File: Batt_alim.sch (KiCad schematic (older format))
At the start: 4 parts

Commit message: added battery footprint
and some net names
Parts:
- BT?: footprint (none) -> Battery:BatteryHolder_Keystone_1042_1x18650
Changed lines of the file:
@@
 F 0 "BT?" H 4718 3896 50  0000 L CNN
 F 1 "Battery_Cell" H 4718 3805 50  0000 L CNN
-F 2 "" V 4600 3860 50  0001 C CNN
+F 2 "Battery:BatteryHolder_Keystone_1042_1x18650" V 4600 3860 50  0001 C CNN
 F 3 "~" V 4600 3860 50  0001 C CNN
 	1    4600 3800

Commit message: fin schéma, début placement
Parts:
- gave numbers to parts that had none: 4
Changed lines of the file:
@@
 $EndDescr
 $Comp
-L Chimere:Batt_Alim U?
+L Chimere:Batt_Alim U4
 U 1 1 5FDF7692
 P 6300 3750
-F 0 "U?" H 6300 4290 50  0000 C CNN
+F 0 "U4" H 6300 4290 50  0000 C CNN
 F 1 "Batt_Alim" H 6300 4199 50  0000 C CNN
 F 2 "Chimere:Batt_Alim" H 6300 3750 50  0001 C CNN
@@
 	5325 3700 5800 3700
 $Comp
-L Connector_Generic:Conn_01x03 J?
+L Connector_Generic:Conn_01x03 J28
 U 1 1 5FDF9A30
-P 5800 4425
-F 0 "J?" H 5718 4100 50  0000 C CNN
-F 1 "Conn_01x03" H 5718 4191 50  0000 C CNN
-F 2 "Connector_JST:JST_XH_S3B-XH-A_1x03_P2.50mm_Horizontal" H 5800 4425 50  0001 C CNN
-F 3 "~" H 5800 4425 50  0001 C CNN
-	1    5800 4425
-	0    1    1    0
+P 5700 4425
+F 0 "J28" H 5618 4100 50  0000 C CNN
+F 1 "Conn_01x03" H 5618 4191 50  0000 C CNN
+F 2 "Connector_JST:JST_XH_S3B-XH-A_1x03_P2.50mm_Horizontal" H 5700 4425 50  0001 C CNN
+F 3 "~" H 5700 4425 50  0001 C CNN
+	1    5700 4425
+	0    -1   1    0
 $EndComp
-NoConn ~ 5900 4225
 $Comp
 L Connector_Generic:Conn_01x02 J?
@@
 P 5100 3200
 AR Path="/5FC6C772/5FDFAD94" Ref="J?"  Part="1"
-AR Path="/5FC6D1FC/5FDFAD94" Ref="J?"  Part="1"
-F 0 "J?" H 5018 2875 50  0000 C CNN
+AR Path="/5FC6D1FC/5FDFAD94" Ref="J27"  Part="1"
+F 0 "J27" H 5018 2875 50  0000 C CNN
 F 1 "Conn_01x02" H 5018 2966 50  0000 C CNN
 F 2 "Connector_JST:JST_XH_B2B-XH-A_1x02_P2.50mm_Vertical" H 5100 3200 50  0001 C CNN
@@
 	5700 3950 5700 4225
 $Comp
-L Device:Battery_Cell BT?
+L Device:Battery_Cell BT1
 U 1 1 5FDFD2B1
 P 4600 3800
-F 0 "BT?" H 4718 3896 50  0000 L CNN
+F 0 "BT1" H 4718 3896 50  0000 L CNN
 F 1 "Battery_Cell" H 4718 3805 50  0000 L CNN
 F 2 "Battery:BatteryHolder_Keystone_1042_1x18650" V 4600 3860 50  0001 C CNN
@@
 Wire Wire Line
 	5325 3825 5800 3825
+NoConn ~ 5600 4225
 $EndSCHEMATC

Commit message: routing + generation gerber
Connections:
- net labels added: V_ext
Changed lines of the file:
@@
 L Connector_Generic:Conn_01x03 J28
 U 1 1 5FDF9A30
-P 5700 4425
-F 0 "J28" H 5618 4100 50  0000 C CNN
-F 1 "Conn_01x03" H 5618 4191 50  0000 C CNN
-F 2 "Connector_JST:JST_XH_S3B-XH-A_1x03_P2.50mm_Horizontal" H 5700 4425 50  0001 C CNN
-F 3 "~" H 5700 4425 50  0001 C CNN
-	1    5700 4425
-	0    -1   1    0
+P 5800 4425
+F 0 "J28" H 5718 4100 50  0000 C CNN
+F 1 "Conn_01x03" H 5718 4191 50  0000 C CNN
+F 2 "Connector_JST:JST_XH_S3B-XH-A_1x03_P2.50mm_Horizontal" H 5800 4425 50  0001 C CNN
+F 3 "~" H 5800 4425 50  0001 C CNN
+	1    5800 4425
+	0    1    1    0
 $EndComp
 $Comp
@@
 Wire Wire Line
 	5325 3825 5800 3825
-NoConn ~ 5600 4225
+NoConn ~ 5900 4225
+Text Label 5575 3100 0    50   ~ 0
+V_ext
 $EndSCHEMATC

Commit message: maj
simplification dfr
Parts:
- removed BT1: Battery_Cell, Battery:BatteryHolder_Keystone_1042_1x18650, symbol Device:Battery_Cell
- removed J28: Conn_01x03, Connector_JST:JST_XH_S3B-XH-A_1x03_P2.50mm_Horizontal, symbol Connector_Generic:Conn_01x03
- added J4, J9: Conn_01x02, Connector_JST:JST_XH_B2B-XH-A_1x02_P2.50mm_Vertical, symbol Connector_Generic:Conn_01x02
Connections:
- net labels removed: 3V3, V_2_uC, uC_2_V
- wire segments 19 -> 8
- no-connect marks 1 -> 0
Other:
- note added: "G3T12AH-R"
- note added: "connecteur batterie\n"
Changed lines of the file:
@@
 $Descr A4 11693 8268
 encoding utf-8
-Sheet 5 5
+Sheet 5 6
 Title ""
 Date ""
@@
 	1    0    0    -1
 $EndComp
-Text GLabel 6950 3575 2    50   Input ~ 0
-GND
 Text GLabel 6950 3450 2    50   Input ~ 0
 5V
 Wire Wire Line
 	6800 3450 6950 3450
-Text GLabel 6950 4075 2    50   Input ~ 0
-GND
 Text GLabel 5700 3575 0    50   Input ~ 0
 GND
 Wire Wire Line
-	6800 3575 6950 3575
-Wire Wire Line
-	6800 4075 6950 4075
-Wire Wire Line
 	5700 3575 5800 3575
-Text GLabel 6950 3825 2    50   Input ~ 0
-V_2_uC
-Text GLabel 6950 3950 2    50   Input ~ 0
-uC_2_V
-Wire Wire Line
-	6800 3825 6950 3825
-Wire Wire Line
-	6800 3950 6950 3950
-Text GLabel 6950 3700 2    50   Input ~ 0
-3V3
-Wire Wire Line
-	6800 3700 6950 3700
-Wire Wire Line
-	5325 3700 5800 3700
-$Comp
-L Connector_Generic:Conn_01x03 J28
-U 1 1 5FDF9A30
-P 5800 4425
-F 0 "J28" H 5718 4100 50  0000 C CNN
-F 1 "Conn_01x03" H 5718 4191 50  0000 C CNN
-F 2 "Connector_JST:JST_XH_S3B-XH-A_1x03_P2.50mm_Horizontal" H 5800 4425 50  0001 C CNN
-F 3 "~" H 5800 4425 50  0001 C CNN
-	1    5800 4425
-	0    1    1    0
-$EndComp
 $Comp
 L Connector_Generic:Conn_01x02 J?
@@
 Text Notes 3675 3175 0    50   ~ 0
 connecteur alimentation extérieure
-Text Notes 6050 4700 2    50   ~ 0
+Text Notes 5750 4175 2    50   ~ 0
 connecteur interrupteur
-Wire Wire Line
-	5800 4075 5800 4225
-Wire Wire Line
-	5800 3950 5700 3950
-Wire Wire Line
-	5700 3950 5700 4225
-$Comp
-L Device:Battery_Cell BT1
-U 1 1 5FDFD2B1
-P 4600 3800
-F 0 "BT1" H 4718 3896 50  0000 L CNN
-F 1 "Battery_Cell" H 4718 3805 50  0000 L CNN
-F 2 "Battery:BatteryHolder_Keystone_1042_1x18650" V 4600 3860 50  0001 C CNN
-F 3 "~" V 4600 3860 50  0001 C CNN
-	1    4600 3800
-	1    0    0    -1
-$EndComp
-Wire Wire Line
-	4600 3600 5325 3600
-Wire Wire Line
-	5325 3600 5325 3700
-Wire Wire Line
-	4600 3900 5325 3900
-Wire Wire Line
-	5325 3900 5325 3825
-Wire Wire Line
-	5325 3825 5800 3825
-NoConn ~ 5900 4225
 Text Label 5575 3100 0    50   ~ 0
 V_ext
+Text Notes 5900 4175 0    50   ~ 0
+G3T12AH-R
+$Comp
+L Connector_Generic:Conn_01x02 J?
+U 1 1 6031A76D
+P 5500 3900
+AR Path="/5FC6C772/6031A76D" Ref="J?"  Part="1"
+AR Path="/5FC6D1FC/6031A76D" Ref="J9"  Part="1"
+F 0 "J9" H 5418 3575 50  0000 C CNN
+F 1 "Conn_01x02" H 5418 3666 50  0000 C CNN
+F 2 "Connector_JST:JST_XH_B2B-XH-A_1x02_P2.50mm_Vertical" H 5500 3900 50  0001 C CNN
+F 3 "~" H 5500 3900 50  0001 C CNN
+	1    5500 3900
+	0    1    1    0
+$EndComp
+$Comp
+L Connector_Generic:Conn_01x02 J?
+U 1 1 6031BF0F
+P 4550 3800
+AR Path="/5FC6C772/6031BF0F" Ref="J?"  Part="1"
+AR Path="/5FC6D1FC/6031BF0F" Ref="J4"  Part="1"
+F 0 "J4" H 4468 3475 50  0000 C CNN
+F 1 "Conn_01x02" H 4468 3566 50  0000 C CNN
+F 2 "Connector_JST:JST_XH_B2B-XH-A_1x02_P2.50mm_Vertical" H 4550 3800 50  0001 C CNN
+F 3 "~" H 4550 3800 50  0001 C CNN
+	1    4550 3800
+	-1   0    0    1
+$EndComp
+Text Notes 3700 3775 0    50   ~ 0
+connecteur batterie\n
+Text GLabel 4850 3800 2    50   Input ~ 0
+GND
+Wire Wire Line
+	5800 3700 5500 3700
+Wire Wire Line
+	5400 3700 4750 3700
+Wire Wire Line
+	4750 3800 4850 3800
 $EndSCHEMATC

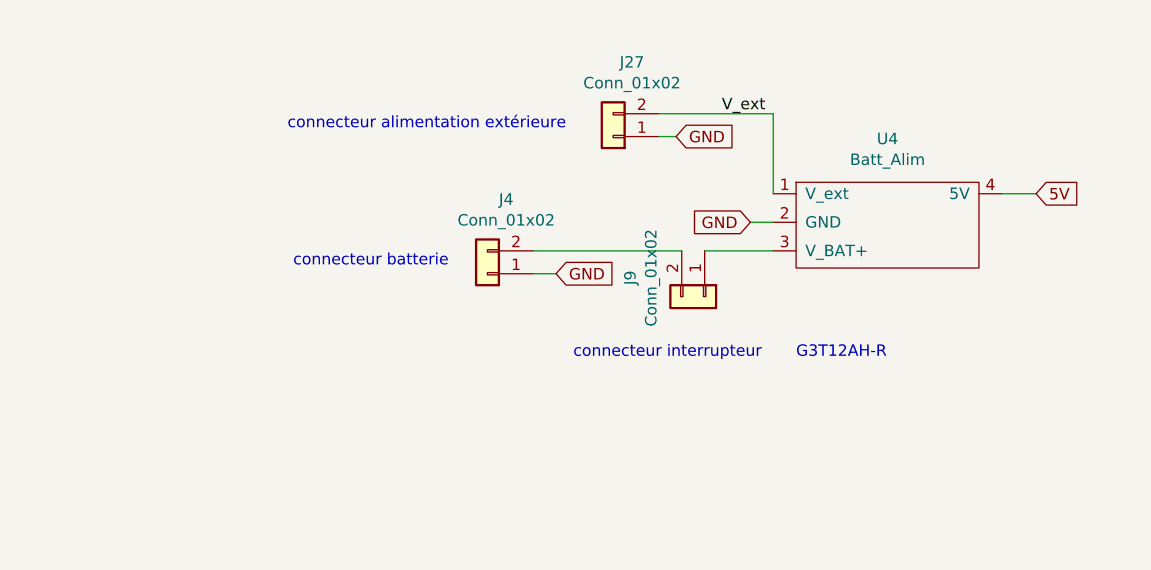
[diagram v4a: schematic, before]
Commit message: changement connecteur
utilisation d'un connecteur usb micro pour l'alimentation
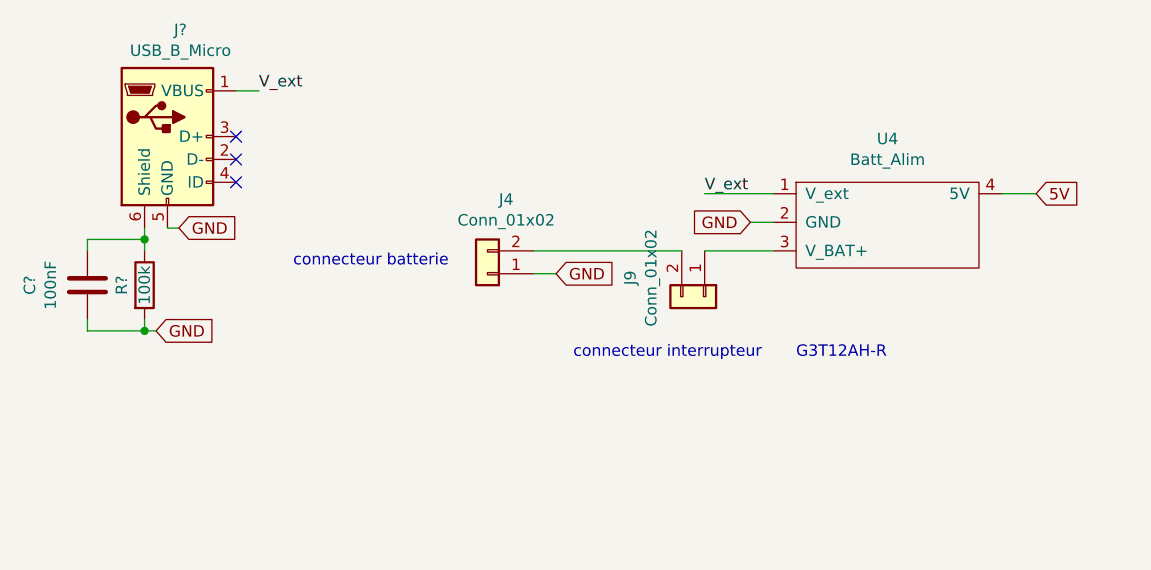
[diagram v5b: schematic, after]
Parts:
- removed J27: Conn_01x02, Connector_JST:JST_XH_B2B-XH-A_1x02_P2.50mm_Vertical, symbol Connector_Generic:Conn_01x02
- added C?: 100nF, Capacitor_SMD:C_0603_1608Metric_Pad1.05x0.95mm_HandSolder, symbol Device:C
- added J?: USB_B_Micro, Connector_USB:USB_Micro-B_Wuerth_629105150521_CircularHoles, symbol Connector:USB_B_Micro
- added R?: 100k, Resistor_SMD:R_0603_1608Metric_Pad1.05x0.95mm_HandSolder, symbol Device:R
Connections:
- net GND: now also C?.2, J?.5 (GND), R?.2
- net V_ext: now also J?.1 (VBUS)
- new net: C?.1, J?.6 (Shield), R?.1
- no-connect marks 0 -> 3
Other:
- note removed: "connecteur alimentation extérieure"
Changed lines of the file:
@@
 Wire Wire Line
 	5700 3575 5800 3575
-$Comp
-L Connector_Generic:Conn_01x02 J?
-U 1 1 5FDFAD94
-P 5100 3200
-AR Path="/5FC6C772/5FDFAD94" Ref="J?"  Part="1"
-AR Path="/5FC6D1FC/5FDFAD94" Ref="J27"  Part="1"
-F 0 "J27" H 5018 2875 50  0000 C CNN
-F 1 "Conn_01x02" H 5018 2966 50  0000 C CNN
-F 2 "Connector_JST:JST_XH_B2B-XH-A_1x02_P2.50mm_Vertical" H 5100 3200 50  0001 C CNN
-F 3 "~" H 5100 3200 50  0001 C CNN
-	1    5100 3200
-	-1   0    0    1
-$EndComp
-Text GLabel 5375 3200 2    50   Input ~ 0
-GND
-Wire Wire Line
-	5300 3200 5375 3200
-Wire Wire Line
-	5300 3100 5800 3100
-Wire Wire Line
-	5800 3100 5800 3450
-Text Notes 3675 3175 0    50   ~ 0
-connecteur alimentation extérieure
 Text Notes 5750 4175 2    50   ~ 0
 connecteur interrupteur
-Text Label 5575 3100 0    50   ~ 0
+Text Label 5500 3450 0    50   ~ 0
 V_ext
 Text Notes 5900 4175 0    50   ~ 0
@@
 Wire Wire Line
 	4750 3800 4850 3800
+$Comp
+L Device:R R?
+U 1 1 606BFC88
+P 3050 3850
+AR Path="/5FC6D1B4/606BFC88" Ref="R?"  Part="1"
+AR Path="/5FC6C772/606BFC88" Ref="R?"  Part="1"
+AR Path="/5FC6D1FC/606BFC88" Ref="R?"  Part="1"
+F 0 "R?" V 2950 3850 50  0000 C CNN
+F 1 "100k" V 3050 3850 50  0000 C CNN
+F 2 "Resistor_SMD:R_0603_1608Metric_Pad1.05x0.95mm_HandSolder" V 2980 3850 50  0001 C CNN
+F 3 "~" H 3050 3850 50  0001 C CNN
+	1    3050 3850
+	1    0    0    -1
+$EndComp
+$Comp
+L Device:C C?
+U 1 1 606BFC8E
+P 2800 3850
+AR Path="/5FC6C772/606BFC8E" Ref="C?"  Part="1"
+AR Path="/5FC6D1FC/606BFC8E" Ref="C?"  Part="1"
+F 0 "C?" V 2548 3850 50  0000 C CNN
+F 1 "100nF" V 2639 3850 50  0000 C CNN
+F 2 "Capacitor_SMD:C_0603_1608Metric_Pad1.05x0.95mm_HandSolder" H 2838 3700 50  0001 C CNN
+F 3 "C14663" H 2800 3850 50  0001 C CNN
+	1    2800 3850
+	1    0    0    -1
+$EndComp
+Text GLabel 3200 3600 2    50   Input ~ 0
+GND
+Wire Wire Line
+	3150 3600 3200 3600
+Wire Wire Line
+	3050 3700 3050 3650
+Wire Wire Line
+	2800 3700 2800 3650
+Wire Wire Line
+	2800 3650 3050 3650
+Connection ~ 3050 3650
+Wire Wire Line
+	3050 3650 3050 3600
+Wire Wire Line
+	2800 4000 2800 4050
+Wire Wire Line
+	2800 4050 3050 4050
+Wire Wire Line
+	3050 4050 3050 4000
+Text GLabel 3100 4050 2    50   Input ~ 0
+GND
+Wire Wire Line
+	3100 4050 3050 4050
+Connection ~ 3050 4050
+NoConn ~ 3450 3200
+NoConn ~ 3450 3300
+Text Label 3550 3000 0    50   ~ 0
+V_ext
+Wire Wire Line
+	3550 3000 3450 3000
+Wire Wire Line
+	5500 3450 5800 3450
+NoConn ~ 3450 3400
+$Comp
+L Connector:USB_B_Micro J?
+U 1 1 606C5F07
+P 3150 3200
+F 0 "J?" H 3207 3667 50  0000 C CNN
+F 1 "USB_B_Micro" H 3207 3576 50  0000 C CNN
+F 2 "Connector_USB:USB_Micro-B_Wuerth_629105150521_CircularHoles" H 3300 3150 50  0001 C CNN
+F 3 "~" H 3300 3150 50  0001 C CNN
+	1    3150 3200
+	1    0    0    -1
+$EndComp
 $EndSCHEMATC

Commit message: modification audio + alim
utilisation du module Audio_Facile
+ utilisation d'un rotary switch rotary potentiometer
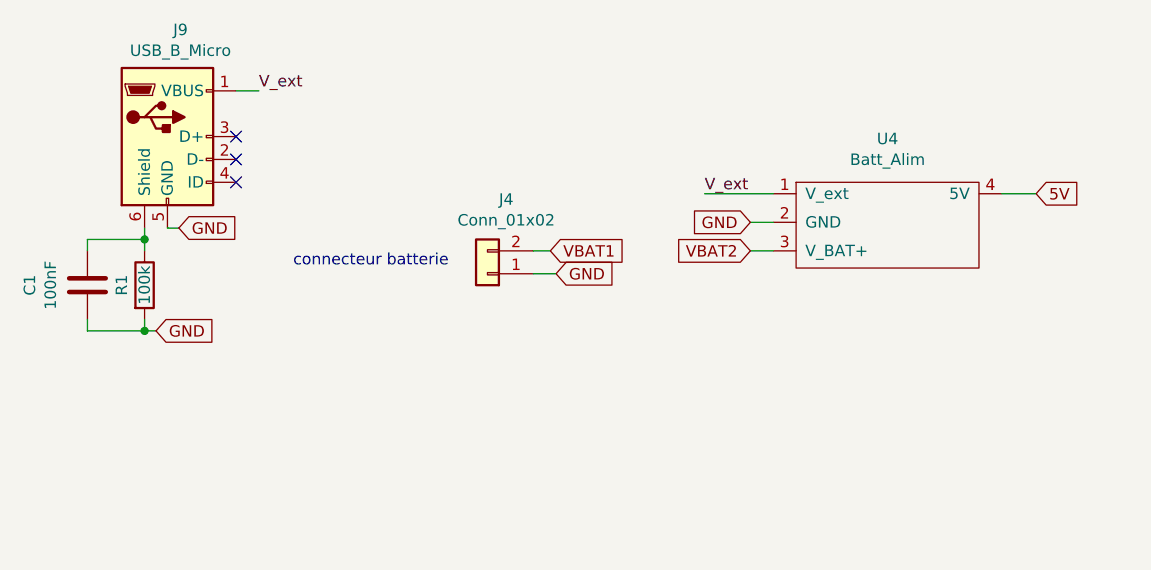
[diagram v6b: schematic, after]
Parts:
- removed J9: Conn_01x02, Connector_JST:JST_XH_B2B-XH-A_1x02_P2.50mm_Vertical, symbol Connector_Generic:Conn_01x02
- gave numbers to parts that had none: 3
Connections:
- net VBAT2: now reaches U4.3 (V_BAT+)
- net VBAT1: now reaches J4.2 (Pin_2)
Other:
- note removed: "G3T12AH-R"
- note removed: "connecteur interrupteur"
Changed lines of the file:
@@
 Wire Wire Line
 	5700 3575 5800 3575
-Text Notes 5750 4175 2    50   ~ 0
-connecteur interrupteur
 Text Label 5500 3450 0    50   ~ 0
 V_ext
-Text Notes 5900 4175 0    50   ~ 0
-G3T12AH-R
-$Comp
-L Connector_Generic:Conn_01x02 J?
-U 1 1 6031A76D
-P 5500 3900
-AR Path="/5FC6C772/6031A76D" Ref="J?"  Part="1"
-AR Path="/5FC6D1FC/6031A76D" Ref="J9"  Part="1"
-F 0 "J9" H 5418 3575 50  0000 C CNN
-F 1 "Conn_01x02" H 5418 3666 50  0000 C CNN
-F 2 "Connector_JST:JST_XH_B2B-XH-A_1x02_P2.50mm_Vertical" H 5500 3900 50  0001 C CNN
-F 3 "~" H 5500 3900 50  0001 C CNN
-	1    5500 3900
-	0    1    1    0
-$EndComp
 $Comp
 L Connector_Generic:Conn_01x02 J?
@@
 GND
 Wire Wire Line
-	5800 3700 5500 3700
-Wire Wire Line
-	5400 3700 4750 3700
-Wire Wire Line
 	4750 3800 4850 3800
 $Comp
@@
 AR Path="/5FC6D1B4/606BFC88" Ref="R?"  Part="1"
 AR Path="/5FC6C772/606BFC88" Ref="R?"  Part="1"
-AR Path="/5FC6D1FC/606BFC88" Ref="R?"  Part="1"
-F 0 "R?" V 2950 3850 50  0000 C CNN
+AR Path="/5FC6D1FC/606BFC88" Ref="R1"  Part="1"
+F 0 "R1" V 2950 3850 50  0000 C CNN
 F 1 "100k" V 3050 3850 50  0000 C CNN
 F 2 "Resistor_SMD:R_0603_1608Metric_Pad1.05x0.95mm_HandSolder" V 2980 3850 50  0001 C CNN
@@
 P 2800 3850
 AR Path="/5FC6C772/606BFC8E" Ref="C?"  Part="1"
-AR Path="/5FC6D1FC/606BFC8E" Ref="C?"  Part="1"
-F 0 "C?" V 2548 3850 50  0000 C CNN
+AR Path="/5FC6D1FC/606BFC8E" Ref="C1"  Part="1"
+F 0 "C1" V 2548 3850 50  0000 C CNN
 F 1 "100nF" V 2639 3850 50  0000 C CNN
 F 2 "Capacitor_SMD:C_0603_1608Metric_Pad1.05x0.95mm_HandSolder" H 2838 3700 50  0001 C CNN
@@
 NoConn ~ 3450 3400
 $Comp
-L Connector:USB_B_Micro J?
+L Connector:USB_B_Micro J9
 U 1 1 606C5F07
 P 3150 3200
-F 0 "J?" H 3207 3667 50  0000 C CNN
+F 0 "J9" H 3207 3667 50  0000 C CNN
 F 1 "USB_B_Micro" H 3207 3576 50  0000 C CNN
 F 2 "Connector_USB:USB_Micro-B_Wuerth_629105150521_CircularHoles" H 3300 3150 50  0001 C CNN
@@
 	1    0    0    -1
 $EndComp
+Text GLabel 4825 3700 2    50   Input ~ 0
+VBAT1
+Text GLabel 5700 3700 0    50   Input ~ 0
+VBAT2
+Wire Wire Line
+	4750 3700 4825 3700
+Wire Wire Line
+	5700 3700 5800 3700
 $EndSCHEMATC

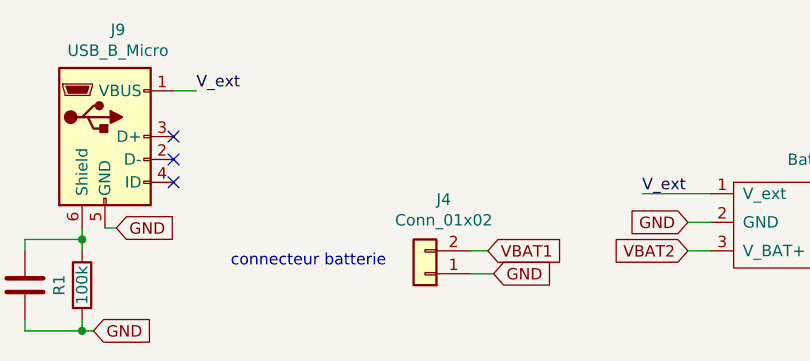
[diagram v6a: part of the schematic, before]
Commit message: chgt connecteur batterie
connecteur batterie JST XH changé pour un PH + inversion des fils. schéma + routage fait
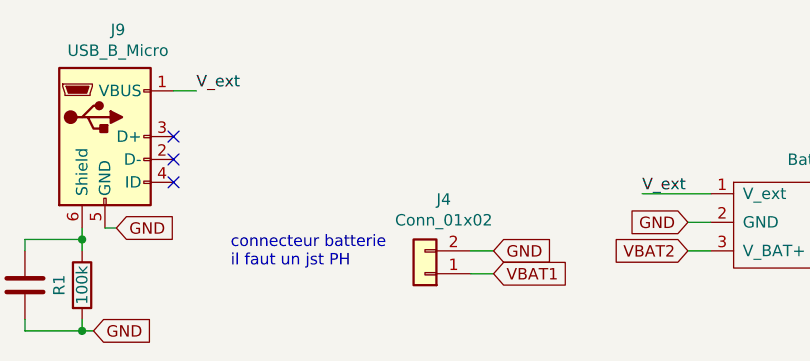
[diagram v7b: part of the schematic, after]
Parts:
- J4: footprint Connector_JST:JST_XH_B2B-XH-A_1x02_P2.50mm_Vertical -> Connector_JST:JST_PH_B2B-PH-K_1x02_P2.00mm_Vertical
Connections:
- net GND: now also J4.2 (Pin_2); no longer J4.1 (Pin_1)
- net VBAT1: now also J4.1 (Pin_1); no longer J4.2 (Pin_2)
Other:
- note added: "connecteur batterie\nil faut un jst PH\n"
- note removed: "connecteur batterie\n"
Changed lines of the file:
@@
 F 0 "J4" H 4468 3475 50  0000 C CNN
 F 1 "Conn_01x02" H 4468 3566 50  0000 C CNN
-F 2 "Connector_JST:JST_XH_B2B-XH-A_1x02_P2.50mm_Vertical" H 4550 3800 50  0001 C CNN
+F 2 "Connector_JST:JST_PH_B2B-PH-K_1x02_P2.00mm_Vertical" H 4550 3800 50  0001 C CNN
 F 3 "~" H 4550 3800 50  0001 C CNN
 	1    4550 3800
@@
 $EndComp
 Text Notes 3700 3775 0    50   ~ 0
-connecteur batterie\n
-Text GLabel 4850 3800 2    50   Input ~ 0
+connecteur batterie\nil faut un jst PH\n
+Text GLabel 4850 3700 2    50   Input ~ 0
 GND
 Wire Wire Line
@@
 	1    0    0    -1
 $EndComp
-Text GLabel 4825 3700 2    50   Input ~ 0
+Text GLabel 4850 3800 2    50   Input ~ 0
 VBAT1
 Text GLabel 5700 3700 0    50   Input ~ 0
 VBAT2
 Wire Wire Line
-	4750 3700 4825 3700
+	5700 3700 5800 3700
 Wire Wire Line
-	5700 3700 5800 3700
+	4750 3700 4850 3700
 $EndSCHEMATC

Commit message: maj split librairie
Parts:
- U4: footprint Chimere:Batt_Alim -> Chimere_mods:Batt_Alim; symbol Chimere:Batt_Alim -> Chimere_mods:Batt_Alim
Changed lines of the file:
@@
 $EndDescr
 $Comp
-L Chimere:Batt_Alim U4
+L Chimere_mods:Batt_Alim U4
 U 1 1 5FDF7692
 P 6300 3750
+AR Path="/5FDF7692" Ref="U4"  Part="1"
+AR Path="/5FC6D1FC/5FDF7692" Ref="U4"  Part="1"
 F 0 "U4" H 6300 4290 50  0000 C CNN
 F 1 "Batt_Alim" H 6300 4199 50  0000 C CNN
-F 2 "Chimere:Batt_Alim" H 6300 3750 50  0001 C CNN
+F 2 "Chimere_mods:Batt_Alim" H 6300 3750 50  0001 C CNN
 F 3 "" H 6300 3750 50  0001 C CNN
 	1    6300 3750
